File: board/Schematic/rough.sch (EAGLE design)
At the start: 14 parts

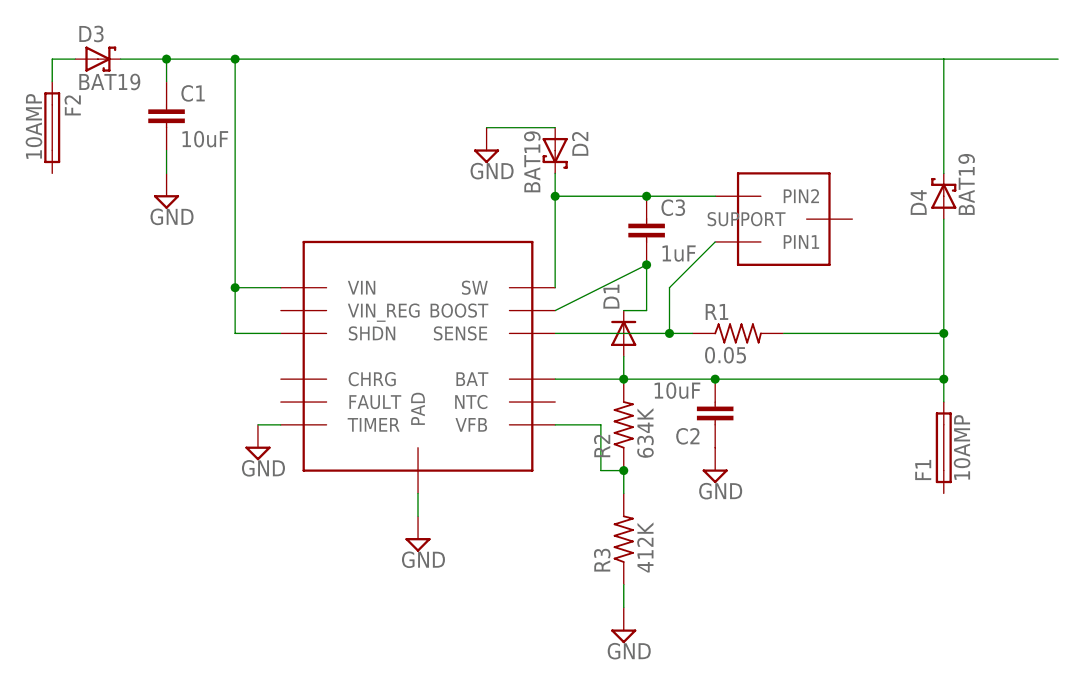
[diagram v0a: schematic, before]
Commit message: finalized board. Gerber files. Board has been ordered
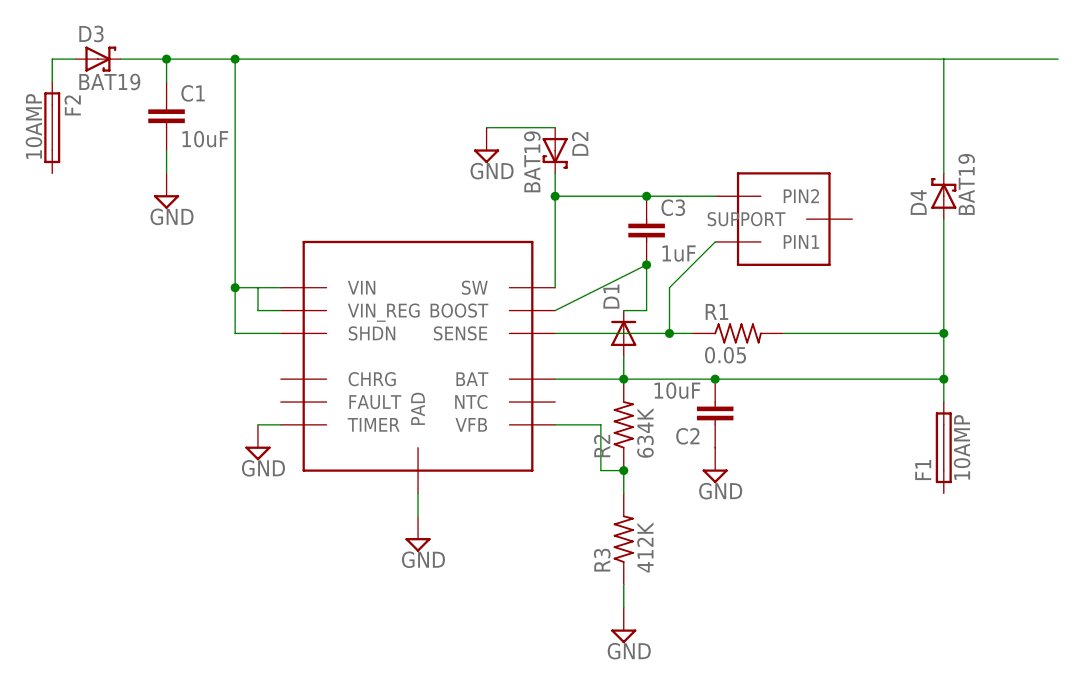
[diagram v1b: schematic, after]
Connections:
- net N$1: now also U$1.VIN_REG
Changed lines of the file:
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@@
 <wire x1="33.02" y1="58.42" x2="38.1" y2="58.42" width="0.1524" layer="91"/>
 <pinref part="U$1" gate="G$2" pin="VIN"/>
-<wire x1="38.1" y1="63.5" x2="33.02" y2="63.5" width="0.1524" layer="91"/>
+<wire x1="38.1" y1="63.5" x2="35.56" y2="63.5" width="0.1524" layer="91"/>
 <junction x="33.02" y="63.5"/>
 <pinref part="D4" gate="1" pin="C"/>
+<wire x1="35.56" y1="63.5" x2="33.02" y2="63.5" width="0.1524" layer="91"/>
 <wire x1="111.76" y1="76.2" x2="111.76" y2="88.9" width="0.1524" layer="91"/>
 <pinref part="D3" gate="1" pin="C"/>
@@
 <junction x="25.4" y="88.9"/>
 <wire x1="111.76" y1="88.9" x2="124.46" y2="88.9" width="0.1524" layer="91"/>
+<pinref part="U$1" gate="G$2" pin="VIN_REG"/>
+<wire x1="38.1" y1="60.96" x2="35.56" y2="60.96" width="0.1524" layer="91"/>
+<wire x1="35.56" y1="60.96" x2="35.56" y2="63.5" width="0.1524" layer="91"/>
 </segment>
 </net>
